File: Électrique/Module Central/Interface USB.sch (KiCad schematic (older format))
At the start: 14 parts, among them J201 USB_B_Mini, U201 FT232RL

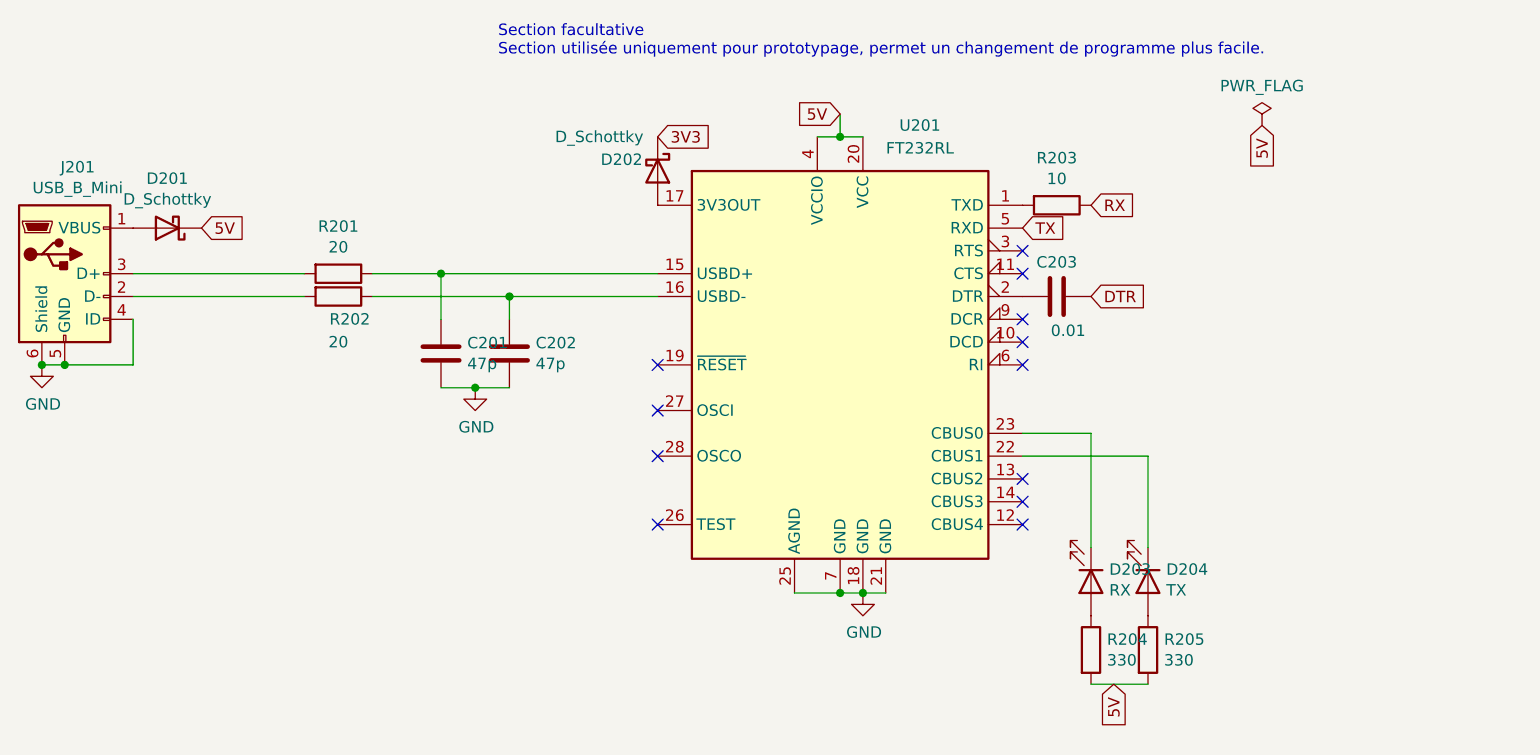
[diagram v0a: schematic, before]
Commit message: Correction des erreurs sur le schéma
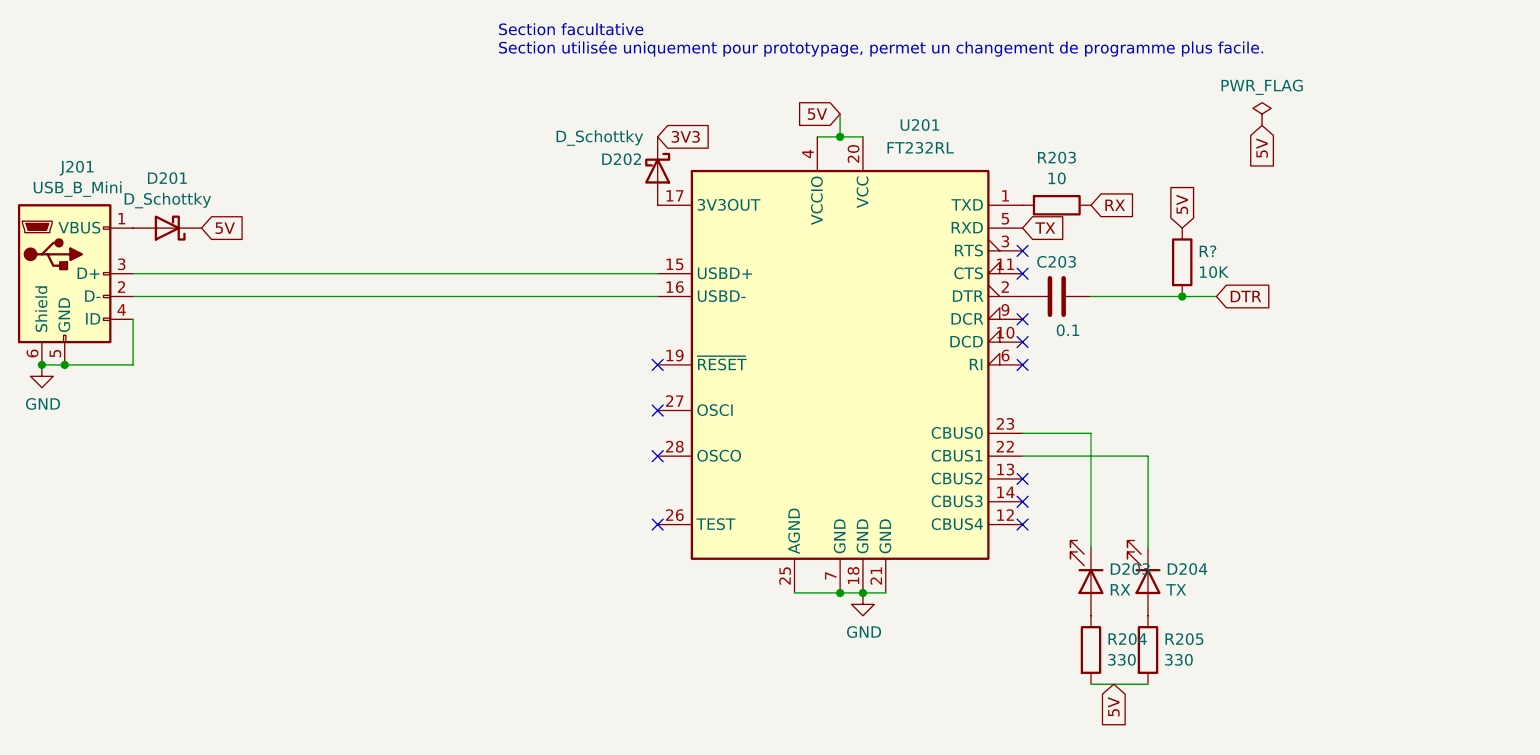
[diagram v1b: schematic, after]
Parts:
- removed C201, C202: 47p, Capacitor_SMD:C_0805_2012Metric, symbol Device:C
- removed R201, R202: 20, Resistor_SMD:R_0805_2012Metric, symbol Device:R
- added R?: 10K, symbol Device:R
- C203: value 0.01 -> 0.1
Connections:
- net 5V: now also R?.1
- net DTR: now also R?.2
- net at U201.15 (USBD+): now also J201.3 (D+)
- net at U201.16 (USBD-): now also J201.2 (D-)
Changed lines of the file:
@@
 Wire Wire Line
 	5650 2700 5650 2800
-Wire Wire Line
-	2550 3500 3300 3500
-Wire Wire Line
-	2550 3400 3300 3400
 $Comp
 L Interface_USB:FT232RL U?
@@
 P 6600 3500
 F 0 "C203" V 6450 3500 50  0000 C CNN
-F 1 "0.01" V 6750 3550 50  0000 C CNN
+F 1 "0.1" V 6750 3550 50  0000 C CNN
 F 2 "Capacitor_SMD:C_0805_2012Metric" H 6638 3350 50  0001 C CNN
 F 3 "~" H 6600 3500 50  0001 C CNN
@@
 	0    1    1    0
 $EndComp
-$Comp
-L Device:R R201
-U 1 1 6009037F
-P 3450 3400
-F 0 "R201" V 3243 3400 50  0000 C CNN
-F 1 "20" V 3334 3400 50  0000 C CNN
-F 2 "Resistor_SMD:R_0805_2012Metric" V 3380 3400 50  0001 C CNN
-F 3 "~" H 3450 3400 50  0001 C CNN
-	1    3450 3400
-	0    1    1    0
-$EndComp
-$Comp
-L Device:R R202
-U 1 1 60090785
-P 3450 3500
-F 0 "R202" V 3550 3550 50  0000 C CNN
-F 1 "20" V 3650 3500 50  0000 C CNN
-F 2 "Resistor_SMD:R_0805_2012Metric" V 3380 3500 50  0001 C CNN
-F 3 "~" H 3450 3500 50  0001 C CNN
-	1    3450 3500
-	0    1    1    0
-$EndComp
-Wire Wire Line
-	3600 3400 3900 3400
-$Comp
-L Device:C C201
-U 1 1 60091934
-P 3900 3750
-F 0 "C201" H 4015 3796 50  0000 L CNN
-F 1 "47p" H 4015 3705 50  0000 L CNN
-F 2 "Capacitor_SMD:C_0805_2012Metric" H 3938 3600 50  0001 C CNN
-F 3 "~" H 3900 3750 50  0001 C CNN
-	1    3900 3750
-	1    0    0    -1
-$EndComp
-Wire Wire Line
-	3600 3500 4200 3500
-$Comp
-L Device:C C202
-U 1 1 60091E2F
-P 4200 3750
-F 0 "C202" H 4315 3796 50  0000 L CNN
-F 1 "47p" H 4315 3705 50  0000 L CNN
-F 2 "Capacitor_SMD:C_0805_2012Metric" H 4238 3600 50  0001 C CNN
-F 3 "~" H 4200 3750 50  0001 C CNN
-	1    4200 3750
-	1    0    0    -1
-$EndComp
-Wire Wire Line
-	3900 3600 3900 3400
-Connection ~ 3900 3400
-Wire Wire Line
-	3900 3400 4850 3400
-Wire Wire Line
-	4200 3500 4200 3600
-Connection ~ 4200 3500
-Wire Wire Line
-	4200 3500 4850 3500
-$Comp
-L power:GND #PWR0202
-U 1 1 60092785
-P 4050 3900
-F 0 "#PWR0202" H 4050 3650 50  0001 C CNN
-F 1 "GND" H 4055 3727 50  0000 C CNN
-F 2 "" H 4050 3900 50  0001 C CNN
-F 3 "" H 4050 3900 50  0001 C CNN
-	1    4050 3900
-	1    0    0    -1
-$EndComp
-Wire Wire Line
-	3900 3900 4050 3900
-Connection ~ 4050 3900
-Wire Wire Line
-	4050 3900 4200 3900
 Text GLabel 6750 3100 2    50   Input ~ 0
 RX
 Text GLabel 6450 3200 2    50   Input ~ 0
 TX
-Text GLabel 6750 3500 2    50   Input ~ 0
+Text GLabel 7300 3500 2    50   Input ~ 0
 DTR
 Text Notes 4150 2450 0    50   ~ 0
@@
 Text GLabel 7500 2750 3    50   Input ~ 0
 5V
+$Comp
+L Device:R R?
+U 1 1 60372200
+P 7150 3350
+F 0 "R?" H 7220 3396 50  0000 L CNN
+F 1 "10K" H 7220 3305 50  0000 L CNN
+F 2 "" V 7080 3350 50  0001 C CNN
+F 3 "~" H 7150 3350 50  0001 C CNN
+	1    7150 3350
+	1    0    0    -1
+$EndComp
+Wire Wire Line
+	6750 3500 7150 3500
+Connection ~ 7150 3500
+Wire Wire Line
+	7150 3500 7300 3500
+Text GLabel 7150 3200 1    50   Input ~ 0
+5V
+Wire Wire Line
+	2550 3400 4850 3400
+Wire Wire Line
+	2550 3500 4850 3500
 $EndSCHEMATC

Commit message: Modification PCB prete à faire
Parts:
- R201: renamed from R?; footprint (none) -> Resistor_SMD:R_0805_2012Metric
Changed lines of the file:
@@
 5V
 $Comp
-L Device:R R?
+L Device:R R201
 U 1 1 60372200
 P 7150 3350
-F 0 "R?" H 7220 3396 50  0000 L CNN
+F 0 "R201" H 7220 3396 50  0000 L CNN
 F 1 "10K" H 7220 3305 50  0000 L CNN
-F 2 "" V 7080 3350 50  0001 C CNN
+F 2 "Resistor_SMD:R_0805_2012Metric" V 7080 3350 50  0001 C CNN
 F 3 "~" H 7150 3350 50  0001 C CNN
 	1    7150 3350

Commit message: oups
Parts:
- J201: symbol Module-Central-rescue:USB_B_Mini-Connector -> Module-Central-rescue:USB_B_Mini-Connector-Module-Central-rescue
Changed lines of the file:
@@
 Connection ~ 2250 3800
 $Comp
-L Module-Central-rescue:USB_B_Mini-Connector J?
+L Module-Central-rescue:USB_B_Mini-Connector-Module-Central-rescue J?
 U 1 1 600862CF
 P 2250 3400
